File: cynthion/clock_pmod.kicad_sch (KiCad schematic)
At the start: 7 parts, among them IC1 ECP5-BGA256, Y1 Osc60MHz

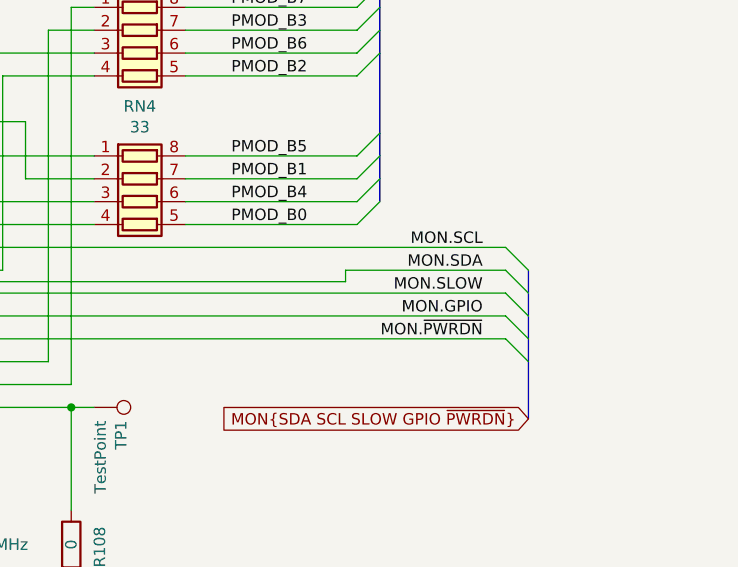
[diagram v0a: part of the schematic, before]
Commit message: hardware: change U1 from WLCSP to VQFN package
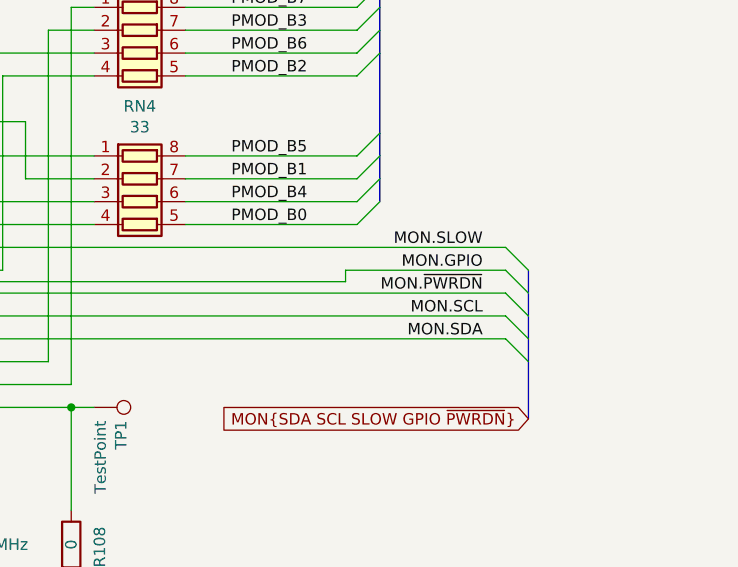
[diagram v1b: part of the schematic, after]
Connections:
- net MON.GPIO: now also IC1.D6 (PT20B); no longer IC1.D7 (PT24B)
- net MON.SCL: now also IC1.D7 (PT24B); no longer IC1.C6 (PT22A)
- net MON.SDA: now also IC1.C7 (PT27A); no longer IC1.D6 (PT20B)
- net MON.SLOW: now also IC1.C6 (PT22A); no longer IC1.D5 (PT13B)
- net MON.~{PWRDN}: now also IC1.D5 (PT13B); no longer IC1.C7 (PT27A)
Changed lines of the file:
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@@
     (effects (font (size 1.27 1.27)) (justify left bottom))
   )
-  (label "MON.SLOW" (at 161.29 107.95 180)
+  (label "MON.SLOW" (at 161.29 102.87 180)
     (effects (font (size 1.27 1.27)) (justify right bottom))
   )
@@
     (effects (font (size 1.27 1.27)) (justify left bottom))
   )
-  (label "MON.SCL" (at 161.29 102.87 180)
+  (label "MON.SCL" (at 161.29 110.49 180)
     (effects (font (size 1.27 1.27)) (justify right bottom))
   )
@@
     (effects (font (size 1.27 1.27)) (justify left bottom))
   )
-  (label "MON.GPIO" (at 161.29 110.49 180)
+  (label "MON.GPIO" (at 161.29 105.41 180)
     (effects (font (size 1.27 1.27)) (justify right bottom))
   )
@@
     (effects (font (size 1.27 1.27)) (justify left bottom))
   )
-  (label "MON.SDA" (at 161.29 105.41 180)
+  (label "MON.SDA" (at 161.29 113.03 180)
     (effects (font (size 1.27 1.27)) (justify right bottom))
   )
-  (label "MON.~{PWRDN}" (at 161.29 113.03 180)
+  (label "MON.~{PWRDN}" (at 161.29 107.95 180)
     (effects (font (size 1.27 1.27)) (justify right bottom))
   )
